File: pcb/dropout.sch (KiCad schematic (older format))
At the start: 59 parts, among them SW1 Rotary_Encoder_Switch, SW2 SW_Push, U1 ProMicro, U2 ProMicro

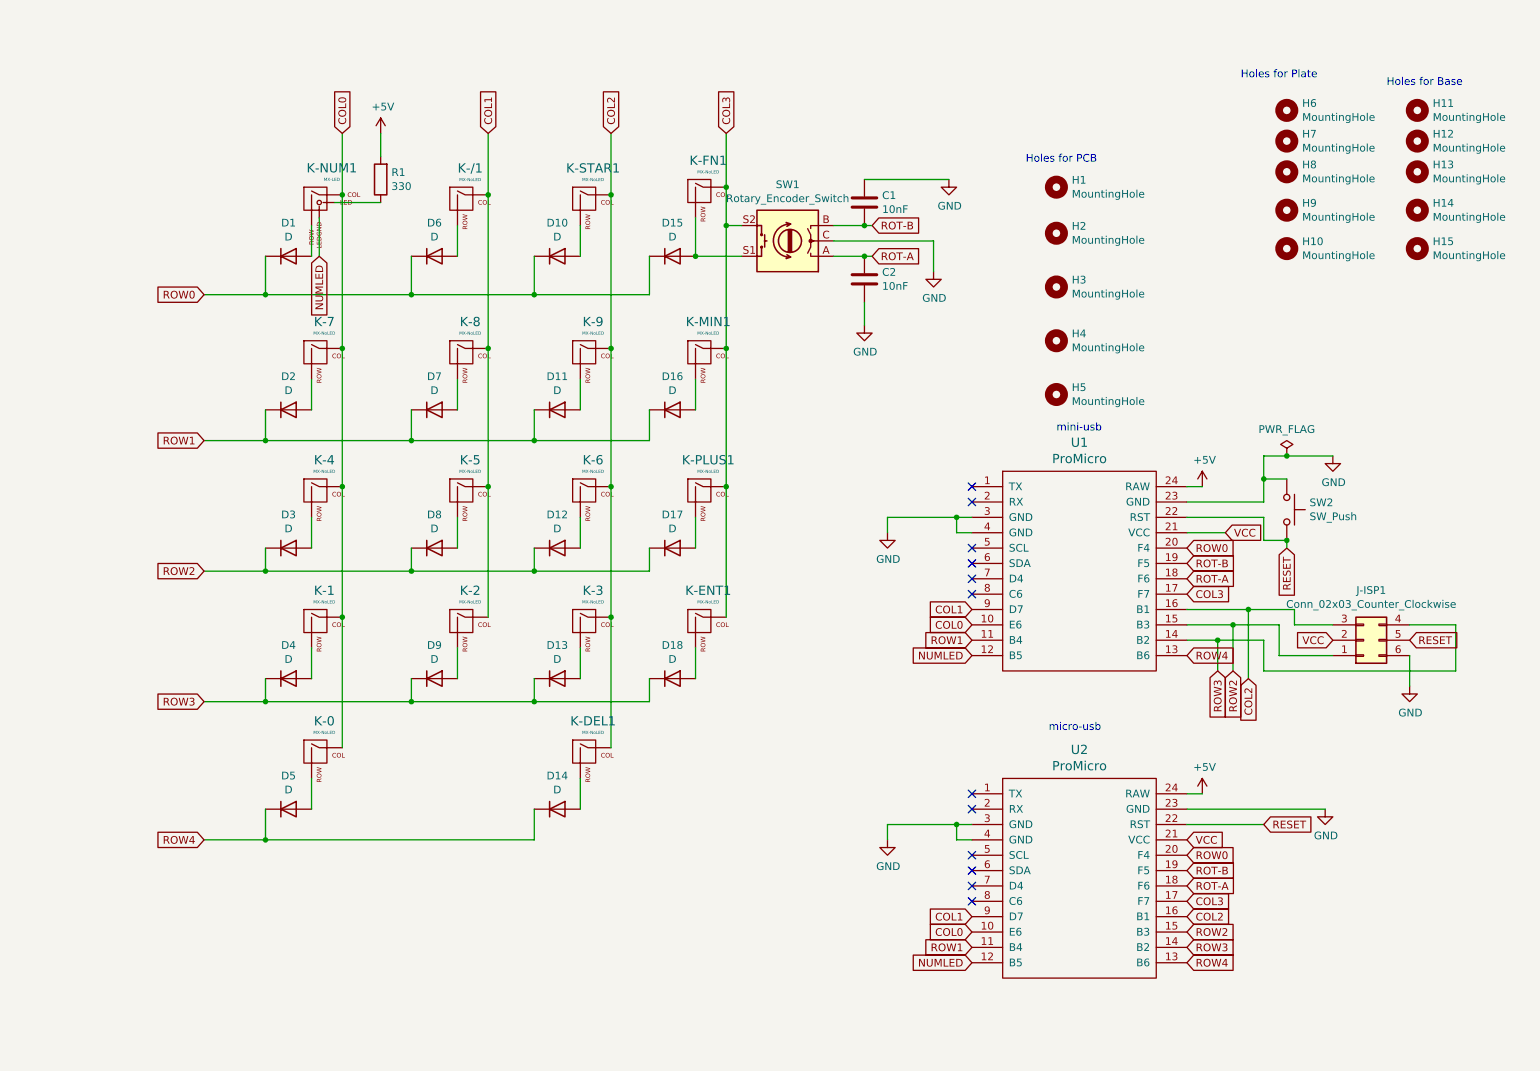
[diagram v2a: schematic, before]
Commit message: i2c trrs connectors
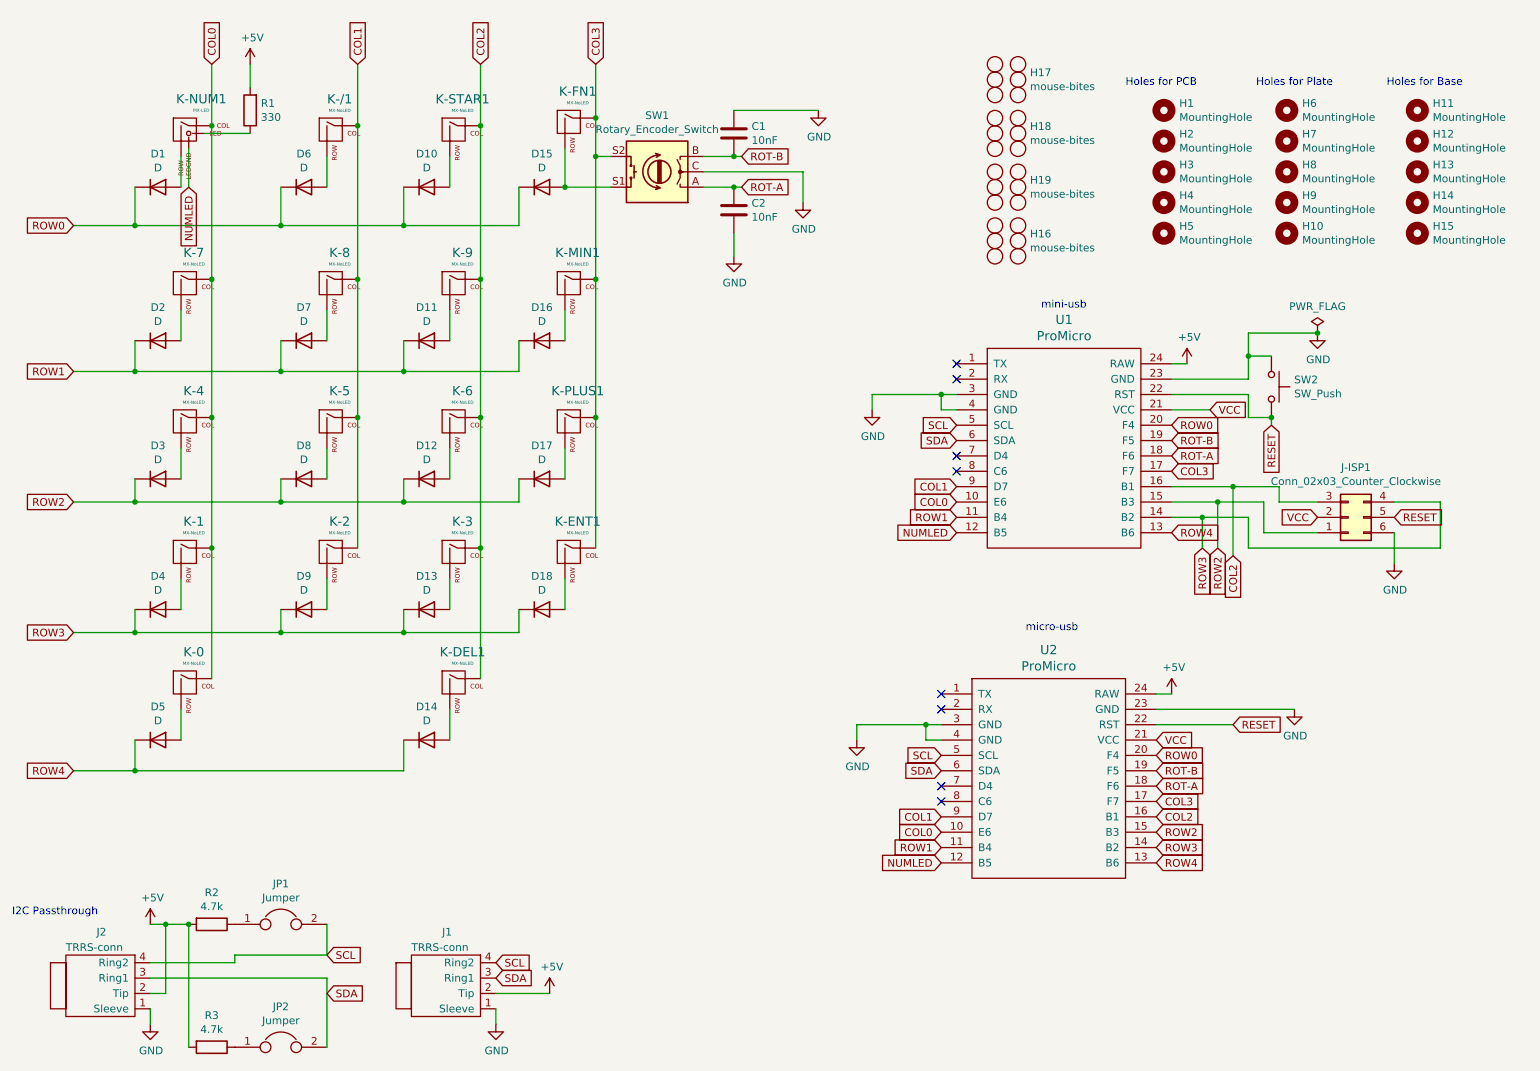
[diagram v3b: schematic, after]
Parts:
- added H16, H17, H18, H19: mouse-bites, Panelization:mouse-bite-2mm-slot, symbol panelization:mouse-bites
- added J1, J2: TRRS-conn, Keebio-Parts:TRRS-PJ-320A, symbol mykeebio:TRRS-conn
- added JP1, JP2: Jumper, Jumper:SolderJumper-2_P1.3mm_Open_Pad1.0x1.5mm, symbol Device:Jumper
- added R2, R3: 4.7k, Resistor_SMD:R_0805_2012Metric_Pad1.15x1.40mm_HandSolder, symbol Device:R
- U1: footprint promicro:ProMicro_MiniUsb -> Keebio-Parts:ArduinoProMicro-Mini-USB
- U2: footprint promicro:ProMicro -> Keebio-Parts:ArduinoProMicro
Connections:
- net +5V: now also J1.2 (Tip), J2.2 (Tip), R2.2, R3.2
- net GND: now also J1.1 (Sleeve), J2.1 (Sleeve)
- net SCL: now reaches U1.5 (SCL)
- net SCL: now also U2.5 (SCL), J1.4 (Ring2), J2.4 (Ring2), JP1.2
- net SDA: now reaches U1.6 (SDA)
- net SDA: now also U2.6 (SDA), J1.3 (Ring1), J2.3 (Ring1), JP2.2
- new net: JP1.1, R2.1
- new net: JP2.1, R3.1
- no-connect marks 12 -> 8
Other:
- note added: "I2C Passthrough"
- moved on the sheet: C1, C2, D1, D10, D11, D12, D13, D14, D15, D16, D17, D18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

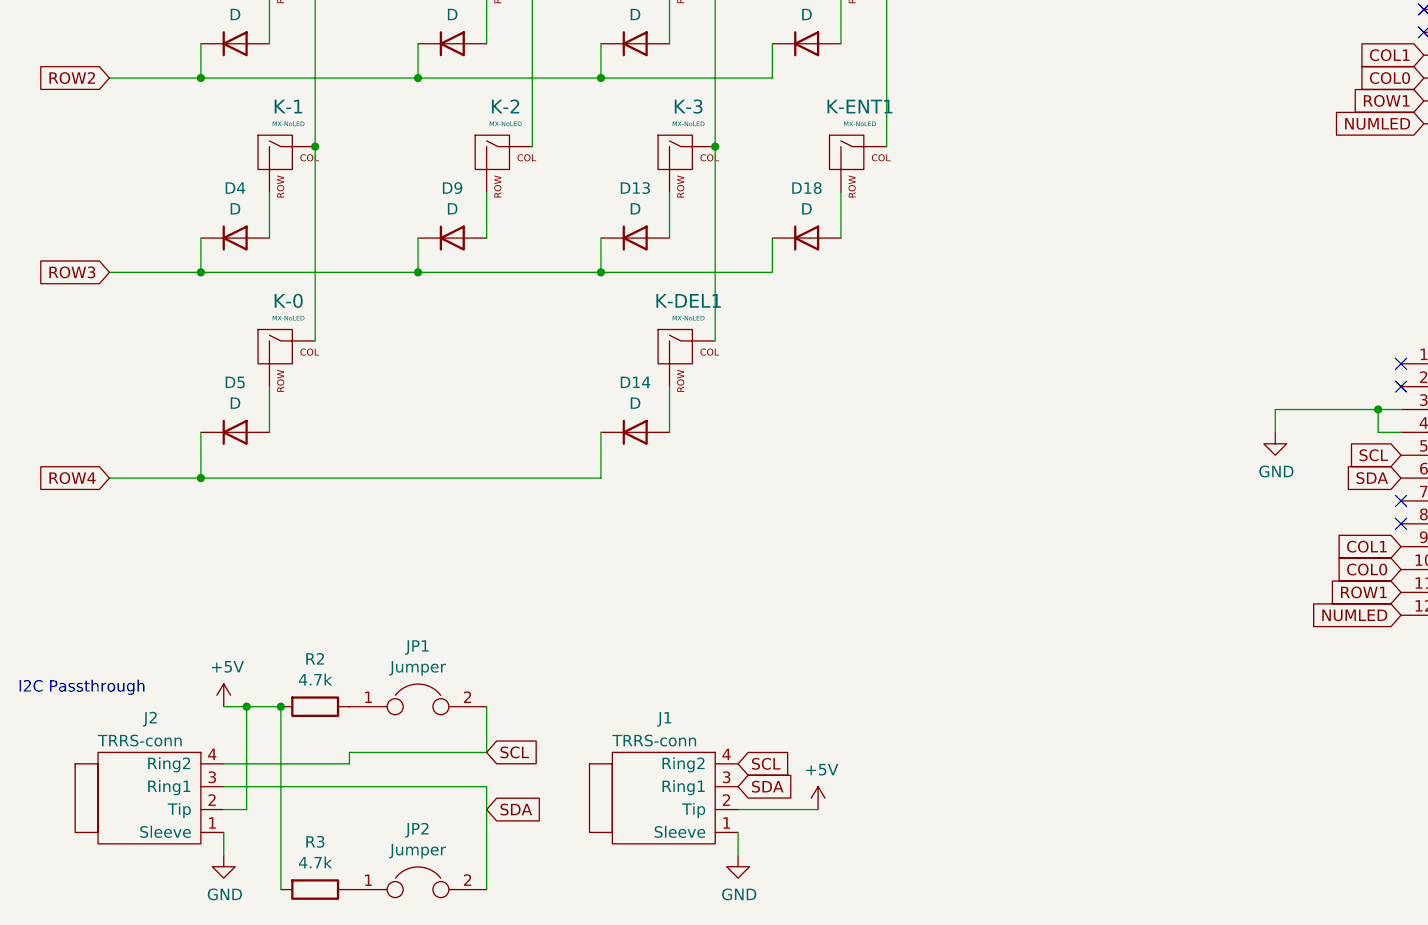
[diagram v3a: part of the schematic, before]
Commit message: replace i2c trrs with header pins
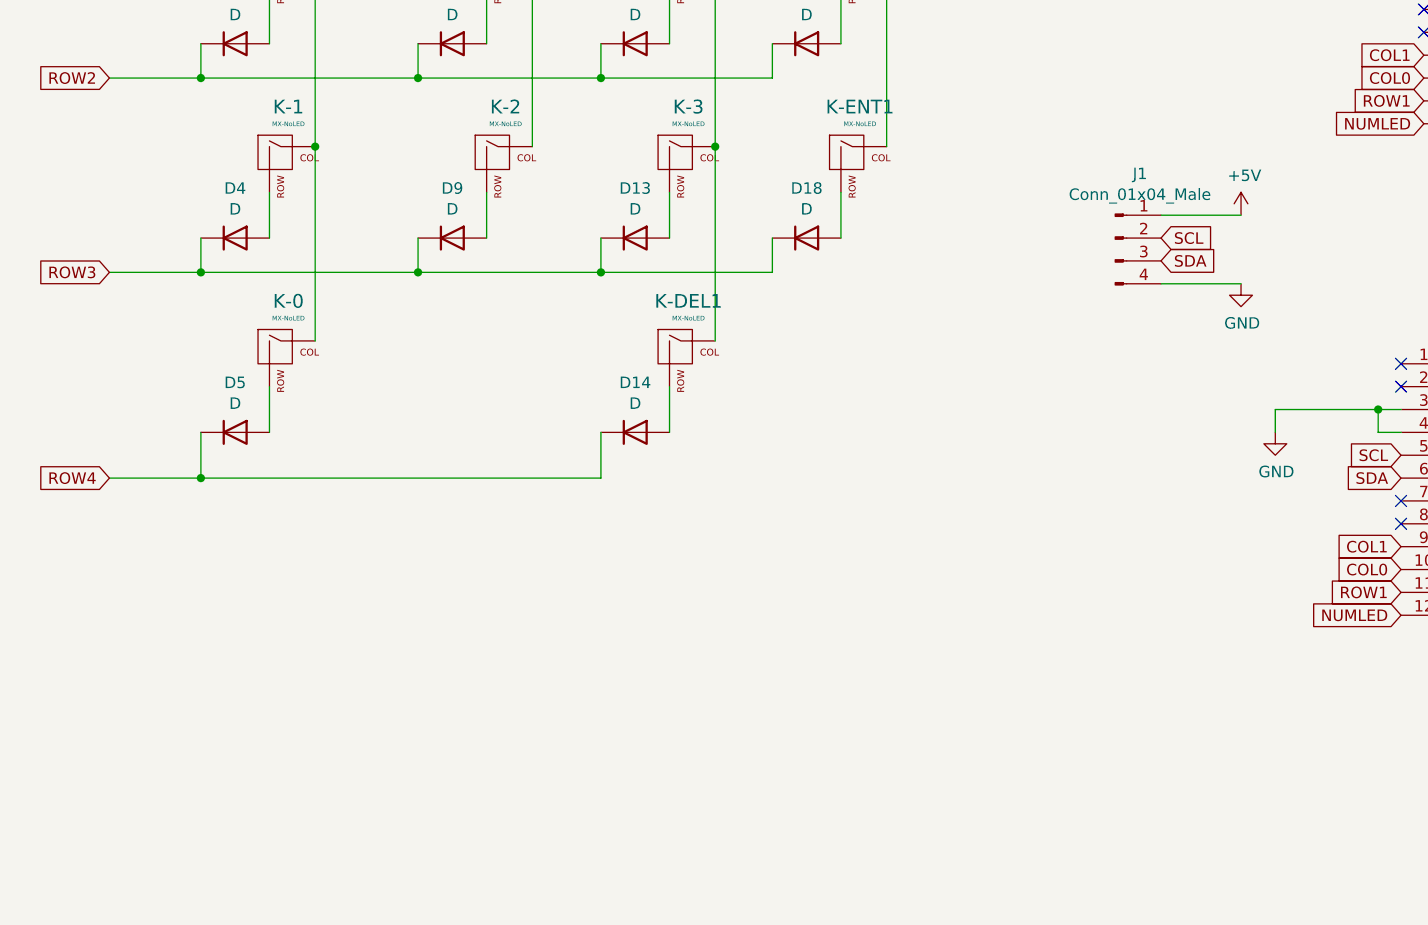
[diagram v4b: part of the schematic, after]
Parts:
- removed J1, J2: TRRS-conn, Keebio-Parts:TRRS-PJ-320A, symbol mykeebio:TRRS-conn
- removed JP1, JP2: Jumper, Jumper:SolderJumper-2_P1.3mm_Open_Pad1.0x1.5mm, symbol Device:Jumper
- removed R2, R3: 4.7k, Resistor_SMD:R_0805_2012Metric_Pad1.15x1.40mm_HandSolder, symbol Device:R
- added J1: Conn_01x04_Male, Connector_PinHeader_2.54mm:PinHeader_1x04_P2.54mm_Vertical, symbol Connector:Conn_01x04_Male
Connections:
- net +5V: now also J1.1 (Pin_1)
- net GND: now also J1.4 (Pin_4)
- net SCL: now also J1.2 (Pin_2)
- net SDA: now also J1.3 (Pin_3)
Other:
- note removed: "I2C Passthrough"
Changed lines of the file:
@@
 Text GLabel 7050 5650 0    50   Input ~ 0
 SDA
-Text GLabel 4150 7000 2    50   Input ~ 0
-SDA
-Text GLabel 4150 6900 2    50   Input ~ 0
-SCL
-$Comp
-L power:+5V #PWR0106
-U 1 1 5FD6C1AA
-P 4500 7100
-F 0 "#PWR0106" H 4500 6950 50  0001 C CNN
-F 1 "+5V" H 4515 7273 50  0000 C CNN
-F 2 "" H 4500 7100 50  0001 C CNN
-F 3 "" H 4500 7100 50  0001 C CNN
-	1    4500 7100
-	1    0    0    -1
-$EndComp
 $Comp
 L power:GND #PWR0104
@@
 F 3 "" H 6500 5450 50  0001 C CNN
 	1    6500 5450
-	1    0    0    -1
-$EndComp
-$Comp
-L power:GND #PWR02
-U 1 1 5FD17E87
-P 4150 7300
-F 0 "#PWR02" H 4150 7050 50  0001 C CNN
-F 1 "GND" H 4155 7127 50  0000 C CNN
-F 2 "" H 4150 7300 50  0001 C CNN
-F 3 "" H 4150 7300 50  0001 C CNN
-	1    4150 7300
 	1    0    0    -1
 $EndComp
@@
 	1    0    0    -1
 $EndComp
-Wire Wire Line
-	4150 7300 4150 7200
-$Comp
-L mykeebio:TRRS-conn J1
-U 1 1 5FE35207
-P 3850 6850
-F 0 "J1" H 3800 7000 50  0000 L CNN
-F 1 "TRRS-conn" H 3600 6900 50  0000 L CNN
-F 2 "Keebio-Parts:TRRS-PJ-320A" H 4000 7050 50  0001 C CNN
-F 3 "" H 4000 7050 50  0001 C CNN
-	1    3850 6850
-	1    0    0    -1
-$EndComp
-Text GLabel 3050 7100 2    50   Input ~ 0
-SDA
-Text GLabel 3050 6850 2    50   Input ~ 0
-SCL
-$Comp
-L power:+5V #PWR0111
-U 1 1 5FE4BEF2
-P 1900 6650
-F 0 "#PWR0111" H 1900 6500 50  0001 C CNN
-F 1 "+5V" H 1915 6823 50  0000 C CNN
-F 2 "" H 1900 6650 50  0001 C CNN
-F 3 "" H 1900 6650 50  0001 C CNN
-	1    1900 6650
-	1    0    0    -1
-$EndComp
-$Comp
-L power:GND #PWR0112
-U 1 1 5FE4BEF8
-P 1900 7300
-F 0 "#PWR0112" H 1900 7050 50  0001 C CNN
-F 1 "GND" H 1905 7127 50  0000 C CNN
-F 2 "" H 1900 7300 50  0001 C CNN
-F 3 "" H 1900 7300 50  0001 C CNN
-	1    1900 7300
-	1    0    0    -1
-$EndComp
-Wire Wire Line
-	1900 7300 1900 7200
-$Comp
-L mykeebio:TRRS-conn J2
-U 1 1 5FE4BF00
-P 1600 6850
-F 0 "J2" H 1550 7000 50  0000 L CNN
-F 1 "TRRS-conn" H 1350 6900 50  0000 L CNN
-F 2 "Keebio-Parts:TRRS-PJ-320A" H 1750 7050 50  0001 C CNN
-F 3 "" H 1750 7050 50  0001 C CNN
-	1    1600 6850
-	1    0    0    -1
-$EndComp
-$Comp
-L Device:R R2
-U 1 1 5FE54CCC
-P 2300 6650
-F 0 "R2" V 2093 6650 50  0000 C CNN
-F 1 "4.7k" V 2184 6650 50  0000 C CNN
-F 2 "Resistor_SMD:R_0805_2012Metric_Pad1.15x1.40mm_HandSolder" V 2230 6650 50  0001 C CNN
-F 3 "~" H 2300 6650 50  0001 C CNN
-	1    2300 6650
-	0    1    1    0
-$EndComp
-$Comp
-L Device:R R3
-U 1 1 5FE5546E
-P 2300 7450
-F 0 "R3" V 2093 7450 50  0000 C CNN
-F 1 "4.7k" V 2184 7450 50  0000 C CNN
-F 2 "Resistor_SMD:R_0805_2012Metric_Pad1.15x1.40mm_HandSolder" V 2230 7450 50  0001 C CNN
-F 3 "~" H 2300 7450 50  0001 C CNN
-	1    2300 7450
-	0    1    1    0
-$EndComp
-Text Notes 1000 6600 0    50   ~ 0
-I2C Passthrough
-$Comp
-L Device:Jumper JP1
-U 1 1 60034A1F
-P 2750 6650
-F 0 "JP1" H 2750 6914 50  0000 C CNN
-F 1 "Jumper" H 2750 6823 50  0000 C CNN
-F 2 "Jumper:SolderJumper-2_P1.3mm_Open_Pad1.0x1.5mm" H 2750 6650 50  0001 C CNN
-F 3 "~" H 2750 6650 50  0001 C CNN
-	1    2750 6650
-	1    0    0    -1
-$EndComp
-$Comp
-L Device:Jumper JP2
-U 1 1 60035A6A
-P 2750 7450
-F 0 "JP2" H 2750 7714 50  0000 C CNN
-F 1 "Jumper" H 2750 7623 50  0000 C CNN
-F 2 "Jumper:SolderJumper-2_P1.3mm_Open_Pad1.0x1.5mm" H 2750 7450 50  0001 C CNN
-F 3 "~" H 2750 7450 50  0001 C CNN
-	1    2750 7450
-	1    0    0    -1
-$EndComp
-Wire Wire Line
-	2450 6850 3050 6850
-Wire Wire Line
-	3050 6850 3050 6650
-Wire Wire Line
-	2150 6650 2150 7450
-Wire Wire Line
-	1900 6650 2000 6650
-Connection ~ 2150 6650
-Wire Wire Line
-	1900 6900 2450 6900
-Wire Wire Line
-	2450 6900 2450 6850
-Wire Wire Line
-	1900 7000 3050 7000
-Wire Wire Line
-	3050 7000 3050 7450
-Wire Wire Line
-	1900 7100 2000 7100
-Wire Wire Line
-	2000 7100 2000 6650
-Connection ~ 2000 6650
-Wire Wire Line
-	2000 6650 2150 6650
-Wire Wire Line
-	4150 7100 4500 7100
 Wire Wire Line
 	4800 1400 4800 1650
@@
 $EndComp
 Connection ~ 9500 2800
+Text GLabel 6000 4600 2    50   Input ~ 0
+SCL
+Text GLabel 6000 4700 2    50   Input ~ 0
+SDA
+$Comp
+L Connector:Conn_01x04_Male J1
+U 1 1 5FD983DA
+P 5800 4600
+F 0 "J1" H 5908 4881 50  0000 C CNN
+F 1 "Conn_01x04_Male" H 5908 4790 50  0000 C CNN
+F 2 "Connector_PinHeader_2.54mm:PinHeader_1x04_P2.54mm_Vertical" H 5800 4600 50  0001 C CNN
+F 3 "~" H 5800 4600 50  0001 C CNN
+	1    5800 4600
+	1    0    0    -1
+$EndComp
+$Comp
+L power:+5V #PWR0106
+U 1 1 5FD99212
+P 6350 4500
+F 0 "#PWR0106" H 6350 4350 50  0001 C CNN
+F 1 "+5V" H 6365 4673 50  0000 C CNN
+F 2 "" H 6350 4500 50  0001 C CNN
+F 3 "" H 6350 4500 50  0001 C CNN
+	1    6350 4500
+	1    0    0    -1
+$EndComp
+$Comp
+L power:GND #PWR0111
+U 1 1 5FD99D5A
+P 6350 4800
+F 0 "#PWR0111" H 6350 4550 50  0001 C CNN
+F 1 "GND" H 6355 4627 50  0000 C CNN
+F 2 "" H 6350 4800 50  0001 C CNN
+F 3 "" H 6350 4800 50  0001 C CNN
+	1    6350 4800
+	1    0    0    -1
+$EndComp
+Wire Wire Line
+	6000 4800 6350 4800
+Wire Wire Line
+	6000 4500 6350 4500
 $EndSCHEMATC

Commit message: updating to rev0.5
updating to rev0.5
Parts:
- removed J-ISP1: Conn_02x03_Counter_Clockwise, Connector_PinHeader_2.54mm:PinHeader_2x03_P2.54mm_Vertical, symbol Connector_Generic:Conn_02x03_Counter_Clockwise
- removed J1: Conn_01x04_Male, Connector_PinHeader_2.54mm:PinHeader_1x04_P2.54mm_Vertical, symbol Connector:Conn_01x04_Male
- removed U2: ProMicro, Keebio-Parts:ArduinoProMicro, symbol promicro:ProMicro
- D1, D10, D11, D12, D13, D14, D15, D16, D17, D18, D2, D3, D4, D5, D6, D7, D8, D9: footprint Diode_SMD:D_SOD-123 -> footprint:Diode_TH_SOD123
- H16, H17, H18, H19: footprint Panelization:mouse-bite-2mm-slot -> Keebio-Parts:breakaway-mousebites
- K-0, K-ENT1: footprint MX_Only:MXOnly-2U-ReversedStabilizers -> MX_Only:MXOnly-2U-ReversedStabilizers-NoLED
- U1: footprint Keebio-Parts:ArduinoProMicro-Mini-USB -> promicro:ProMico_mini&micro
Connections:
- net RESET: no longer names the net of SW2.2, U1.22 (RST)
- net SCL: no longer names the net of U1.5 (SCL)
- net SDA: no longer names the net of U1.6 (SDA)
- net VCC: no longer names the net of U1.21 (VCC)
- no-connect marks 8 -> 7
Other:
- note removed: "micro-usb\n"
